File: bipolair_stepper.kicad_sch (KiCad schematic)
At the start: 10 parts, among them M901 Stepper_Motor_bipolar, U901 L298HN

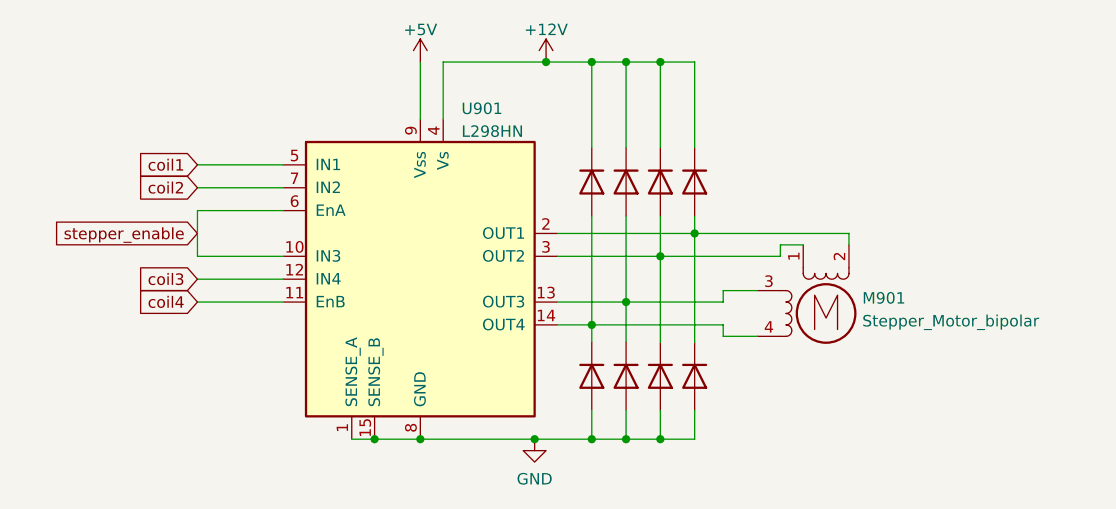
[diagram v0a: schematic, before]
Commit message: added hierarchial labels to some schematics
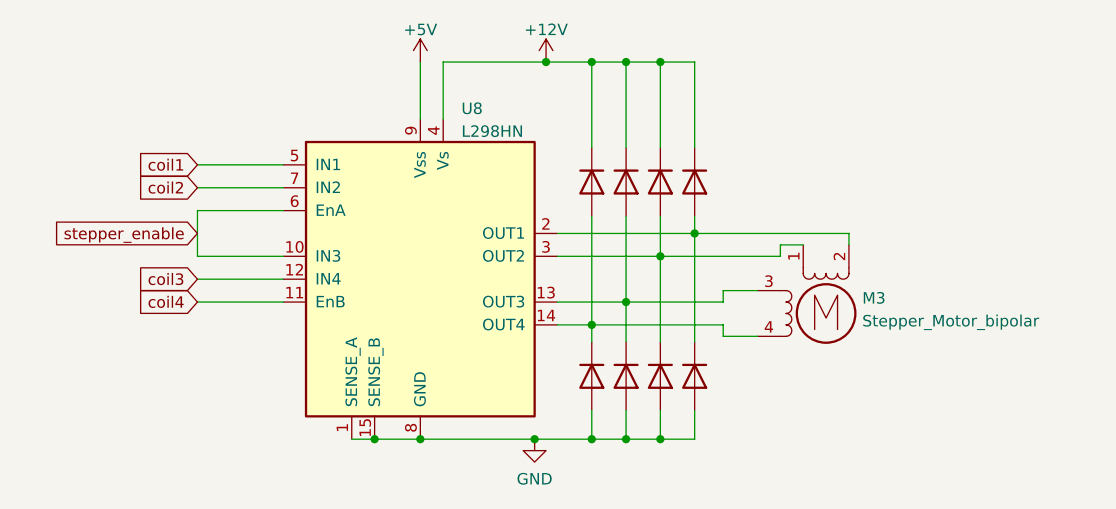
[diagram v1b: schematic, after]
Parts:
- renumbered D901 to D12, D903 to D13, D905 to D14, D907 to D15, D902 to D16, D904 to D17, D906 to D18, D908 to D19, M901 to M3, U901 to U8

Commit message: moved some schematic scheets to their own folders and routed a board with it. This allow for re-use of PCB parts.
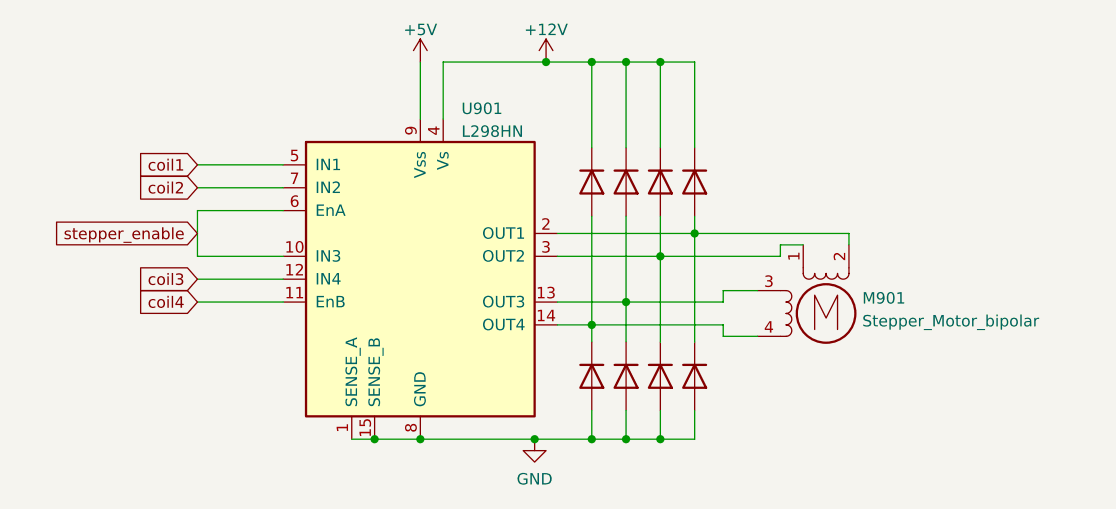
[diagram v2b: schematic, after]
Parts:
- renumbered D12 to D901, D16 to D902, D13 to D903, D17 to D904, D14 to D905, D18 to D906, D15 to D907, D19 to D908, M3 to M901, U8 to U901
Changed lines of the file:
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@@
   (symbol (lib_id "power:+12V") (at 123.825 81.28 0) (unit 1)
     (in_bom yes) (on_board yes) (dnp no) (fields_autoplaced)
-    (property "Reference" "#PWR037" (at 123.825 85.09 0)
+    (property "Reference" "#PWR0124" (at 123.825 85.09 0)
       (effects (font (size 1.27 1.27)) hide)
     )
@@
       (project "general_schematics"
         (path "/e777d9ec-d073-4229-a9e6-2cf85636e407/9c8f6162-972e-4a6a-9072-cbd128d102d4"
-          (reference "#PWR037") (unit 1)
+          (reference "#PWR0124") (unit 1)
         )
       )
@@
   (symbol (lib_id "Motor:Stepper_Motor_bipolar") (at 154.94 109.22 0) (unit 1)
     (in_bom yes) (on_board yes) (dnp no) (fields_autoplaced)
-    (property "Reference" "M3" (at 158.9532 107.5344 0)
+    (property "Reference" "M901" (at 158.9532 107.5344 0)
       (effects (font (size 1.27 1.27)) (justify left))
     )
@@
       (project "general_schematics"
         (path "/e777d9ec-d073-4229-a9e6-2cf85636e407/9c8f6162-972e-4a6a-9072-cbd128d102d4"
-          (reference "M3") (unit 1)
+          (reference "M901") (unit 1)
         )
       )
@@
   (symbol (lib_id "Device:D") (at 128.905 94.615 270) (unit 1)
     (in_bom yes) (on_board yes) (dnp no) (fields_autoplaced)
-    (property "Reference" "D12" (at 130.937 93.7803 90)
+    (property "Reference" "D901" (at 130.937 93.7803 90)
       (effects (font (size 1.27 1.27)) (justify left) hide)
     )
@@
       (project "general_schematics"
         (path "/e777d9ec-d073-4229-a9e6-2cf85636e407/9c8f6162-972e-4a6a-9072-cbd128d102d4"
-          (reference "D12") (unit 1)
+          (reference "D901") (unit 1)
         )
       )
@@
   (symbol (lib_id "Device:D") (at 140.335 94.615 270) (unit 1)
     (in_bom yes) (on_board yes) (dnp no) (fields_autoplaced)
-    (property "Reference" "D15" (at 142.367 93.7803 90)
+    (property "Reference" "D907" (at 142.367 93.7803 90)
       (effects (font (size 1.27 1.27)) (justify left) hide)
     )
@@
       (project "general_schematics"
         (path "/e777d9ec-d073-4229-a9e6-2cf85636e407/9c8f6162-972e-4a6a-9072-cbd128d102d4"
-          (reference "D15") (unit 1)
+          (reference "D907") (unit 1)
         )
       )
@@
   (symbol (lib_id "Device:D") (at 140.335 116.205 270) (unit 1)
     (in_bom yes) (on_board yes) (dnp no) (fields_autoplaced)
-    (property "Reference" "D19" (at 142.367 115.3703 90)
+    (property "Reference" "D908" (at 142.367 115.3703 90)
       (effects (font (size 1.27 1.27)) (justify left) hide)
     )
@@
       (project "general_schematics"
         (path "/e777d9ec-d073-4229-a9e6-2cf85636e407/9c8f6162-972e-4a6a-9072-cbd128d102d4"
-          (reference "D19") (unit 1)
+          (reference "D908") (unit 1)
         )
       )
@@
   (symbol (lib_id "power:GND") (at 122.555 123.19 0) (unit 1)
     (in_bom yes) (on_board yes) (dnp no) (fields_autoplaced)
-    (property "Reference" "#PWR038" (at 122.555 129.54 0)
+    (property "Reference" "#PWR0122" (at 122.555 129.54 0)
       (effects (font (size 1.27 1.27)) hide)
     )
@@
       (project "general_schematics"
         (path "/e777d9ec-d073-4229-a9e6-2cf85636e407/9c8f6162-972e-4a6a-9072-cbd128d102d4"
-          (reference "#PWR038") (unit 1)
+          (reference "#PWR0122") (unit 1)
         )
       )
@@
   (symbol (lib_id "Device:D") (at 136.525 94.615 270) (unit 1)
     (in_bom yes) (on_board yes) (dnp no) (fields_autoplaced)
-    (property "Reference" "D14" (at 138.557 93.7803 90)
+    (property "Reference" "D905" (at 138.557 93.7803 90)
       (effects (font (size 1.27 1.27)) (justify left) hide)
     )
@@
       (project "general_schematics"
         (path "/e777d9ec-d073-4229-a9e6-2cf85636e407/9c8f6162-972e-4a6a-9072-cbd128d102d4"
-          (reference "D14") (unit 1)
+          (reference "D905") (unit 1)
         )
       )
@@
   (symbol (lib_id "Device:D") (at 136.525 116.205 270) (unit 1)
     (in_bom yes) (on_board yes) (dnp no) (fields_autoplaced)
-    (property "Reference" "D18" (at 138.557 115.3703 90)
+    (property "Reference" "D906" (at 138.557 115.3703 90)
       (effects (font (size 1.27 1.27)) (justify left) hide)
     )
@@
       (project "general_schematics"
         (path "/e777d9ec-d073-4229-a9e6-2cf85636e407/9c8f6162-972e-4a6a-9072-cbd128d102d4"
-          (reference "D18") (unit 1)
+          (reference "D906") (unit 1)
         )
       )
@@
   (symbol (lib_id "power:+5V") (at 109.855 81.28 0) (unit 1)
     (in_bom yes) (on_board yes) (dnp no) (fields_autoplaced)
-    (property "Reference" "#PWR036" (at 109.855 85.09 0)
+    (property "Reference" "#PWR0123" (at 109.855 85.09 0)
       (effects (font (size 1.27 1.27)) hide)
     )
@@
       (project "general_schematics"
         (path "/e777d9ec-d073-4229-a9e6-2cf85636e407/9c8f6162-972e-4a6a-9072-cbd128d102d4"
-          (reference "#PWR036") (unit 1)
+          (reference "#PWR0123") (unit 1)
         )
       )
@@
   (symbol (lib_id "Device:D") (at 132.715 94.615 270) (unit 1)
     (in_bom yes) (on_board yes) (dnp no) (fields_autoplaced)
-    (property "Reference" "D13" (at 134.747 93.7803 90)
+    (property "Reference" "D903" (at 134.747 93.7803 90)
       (effects (font (size 1.27 1.27)) (justify left) hide)
     )
@@
       (project "general_schematics"
         (path "/e777d9ec-d073-4229-a9e6-2cf85636e407/9c8f6162-972e-4a6a-9072-cbd128d102d4"
-          (reference "D13") (unit 1)
+          (reference "D903") (unit 1)
         )
       )
@@
   (symbol (lib_id "Device:D") (at 132.715 116.205 270) (unit 1)
     (in_bom yes) (on_board yes) (dnp no) (fields_autoplaced)
-    (property "Reference" "D17" (at 134.747 115.3703 90)
+    (property "Reference" "D904" (at 134.747 115.3703 90)
       (effects (font (size 1.27 1.27)) (justify left) hide)
     )
@@
       (project "general_schematics"
         (path "/e777d9ec-d073-4229-a9e6-2cf85636e407/9c8f6162-972e-4a6a-9072-cbd128d102d4"
-          (reference "D17") (unit 1)
+          (reference "D904") (unit 1)
         )
       )
@@
   (symbol (lib_id "Driver_Motor:L298HN") (at 109.855 105.41 0) (unit 1)
     (in_bom yes) (on_board yes) (dnp no) (fields_autoplaced)
-    (property "Reference" "U8" (at 114.4144 86.4702 0)
+    (property "Reference" "U901" (at 114.4144 86.4702 0)
       (effects (font (size 1.27 1.27)) (justify left))
     )
@@
       (project "general_schematics"
         (path "/e777d9ec-d073-4229-a9e6-2cf85636e407/9c8f6162-972e-4a6a-9072-cbd128d102d4"
-          (reference "U8") (unit 1)
+          (reference "U901") (unit 1)
         )
       )
@@
   (symbol (lib_id "Device:D") (at 128.905 116.205 270) (unit 1)
     (in_bom yes) (on_board yes) (dnp no) (fields_autoplaced)
-    (property "Reference" "D16" (at 130.937 115.3703 90)
+    (property "Reference" "D902" (at 130.937 115.3703 90)
       (effects (font (size 1.27 1.27)) (justify left) hide)
     )
@@
       (project "general_schematics"
         (path "/e777d9ec-d073-4229-a9e6-2cf85636e407/9c8f6162-972e-4a6a-9072-cbd128d102d4"
-          (reference "D16") (unit 1)
-        )
-      )
+          (reference "D902") (unit 1)
+        )
+      )
